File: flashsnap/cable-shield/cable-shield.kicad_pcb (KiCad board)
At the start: 2 copper layers, 47 x 16 mm, 9 parts, among them CN1 CN_6, CN2 CN_6, SW1 SW_PUSH

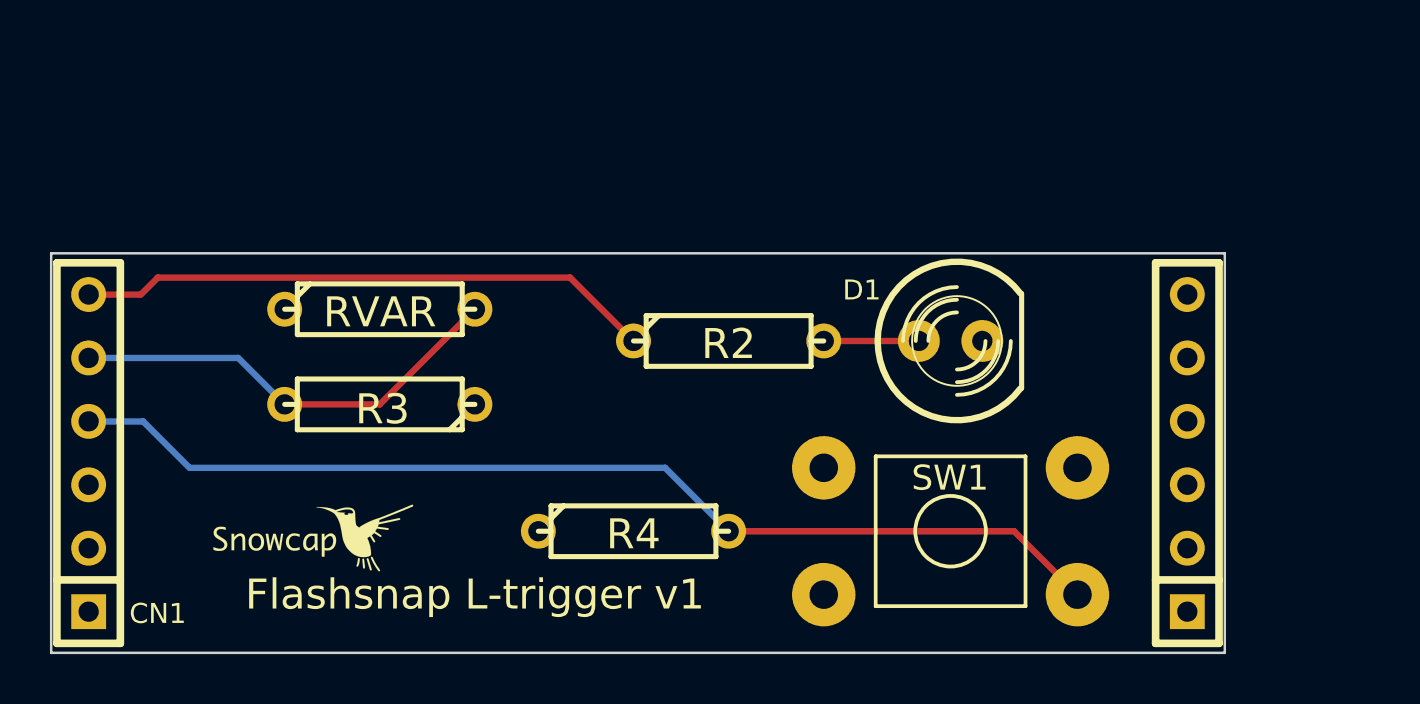
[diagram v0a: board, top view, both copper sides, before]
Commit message: flashsnap: Introduce cable-shield, update others.
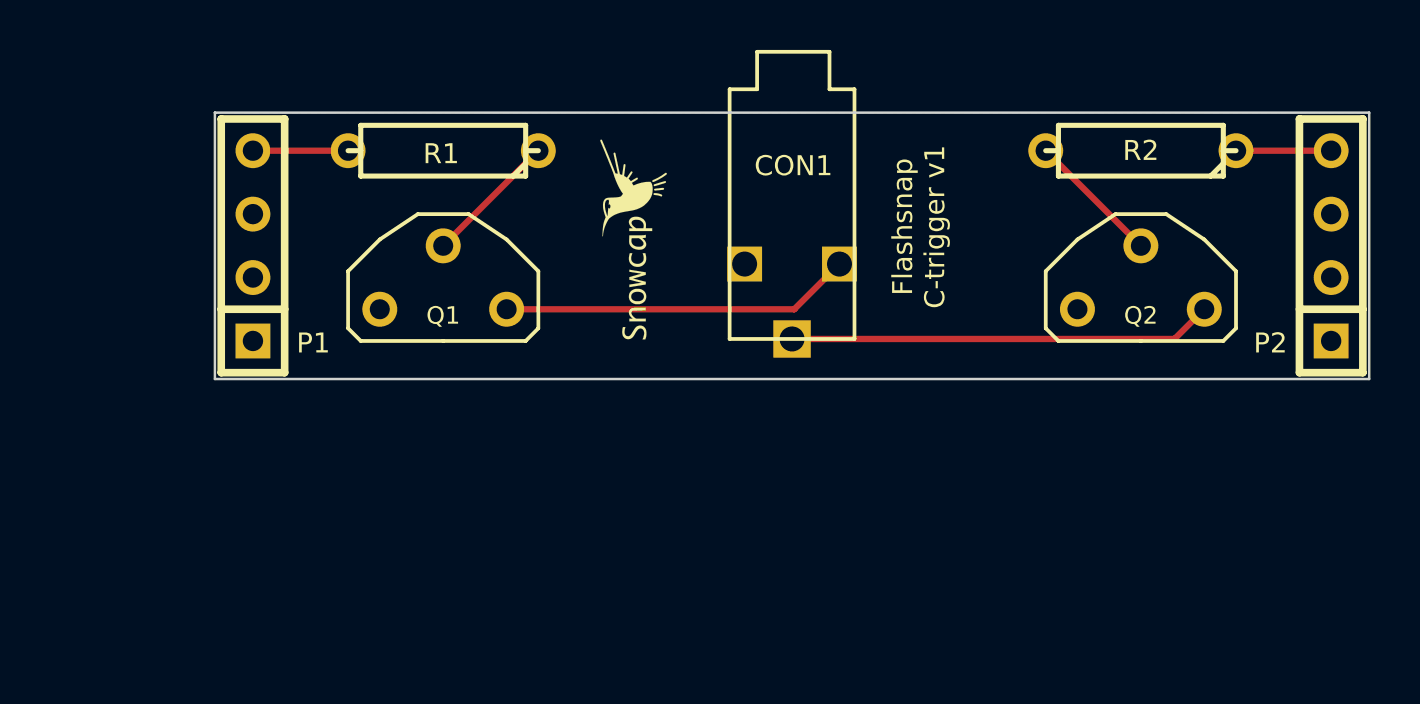
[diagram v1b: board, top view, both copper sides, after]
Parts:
- removed CN1, CN2: CN_6, SIL-6
- removed D1: LED, LED-5MM
- removed R3, R4: R, R3
- removed SW1: SW_PUSH, SW_PUSH_6MM
- added CON1: BARREL_JACK, SJ2.5PC, F.Cu at (217.2, 138.4)
- added P1: CONN_4, SIL-4, F.Cu at (195.6, 139.7)
- added P2: CONN_4, SIL-4, F.Cu at (238.8, 139.7)
- added Q1: NPN, TO92PN-LARGE, F.Cu at (203.2, 139.7)
- added Q2: NPN, TO92PN-LARGE, F.Cu at (231.1, 139.7)
- R1: value RVAR -> R
- moved R2 18.2 mm to (231.1, 135.9), turned to 180 degrees
- moved VAL 17.5 mm to (210.8, 139.4), turned to 90 degrees
- moved R1 6.84 mm to (203.2, 135.9), turned to 180 degrees
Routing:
- net N-000004: track 42.5 -> 0.00 mm
- net N-0000012: track 23.2 -> 3.81 mm
- net N-000003: track 0.00 -> 17.0 mm
- net N-000002: track 0.00 -> 14.1 mm
- net N-0000011: track 17.8 -> 3.81 mm
- net N-0000010: track 0.00 -> 5.39 mm
- net N-000009: track 3.81 -> 5.39 mm
- added copper zone on B.Cu, net N-000001
- removed copper zone on F.Cu, net N-0000010
- removed copper zone on B.Cu, net N-000003
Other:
- board size 47 x 16 mm -> 46.2 x 10.7 mm
- board text added: "Flashsnap C-trigger v1"
- board text removed: "Flashsnap L-trigger v1"
